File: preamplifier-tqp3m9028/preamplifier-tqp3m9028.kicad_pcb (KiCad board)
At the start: 2 copper layers, 35 x 35 mm, 19 parts, among them J101 Barrel_Jack_Switch, J102 Conn_Coaxial, J103 Conn_Coaxial, U101 AMS1117-5.0, U102 TQP3M9028

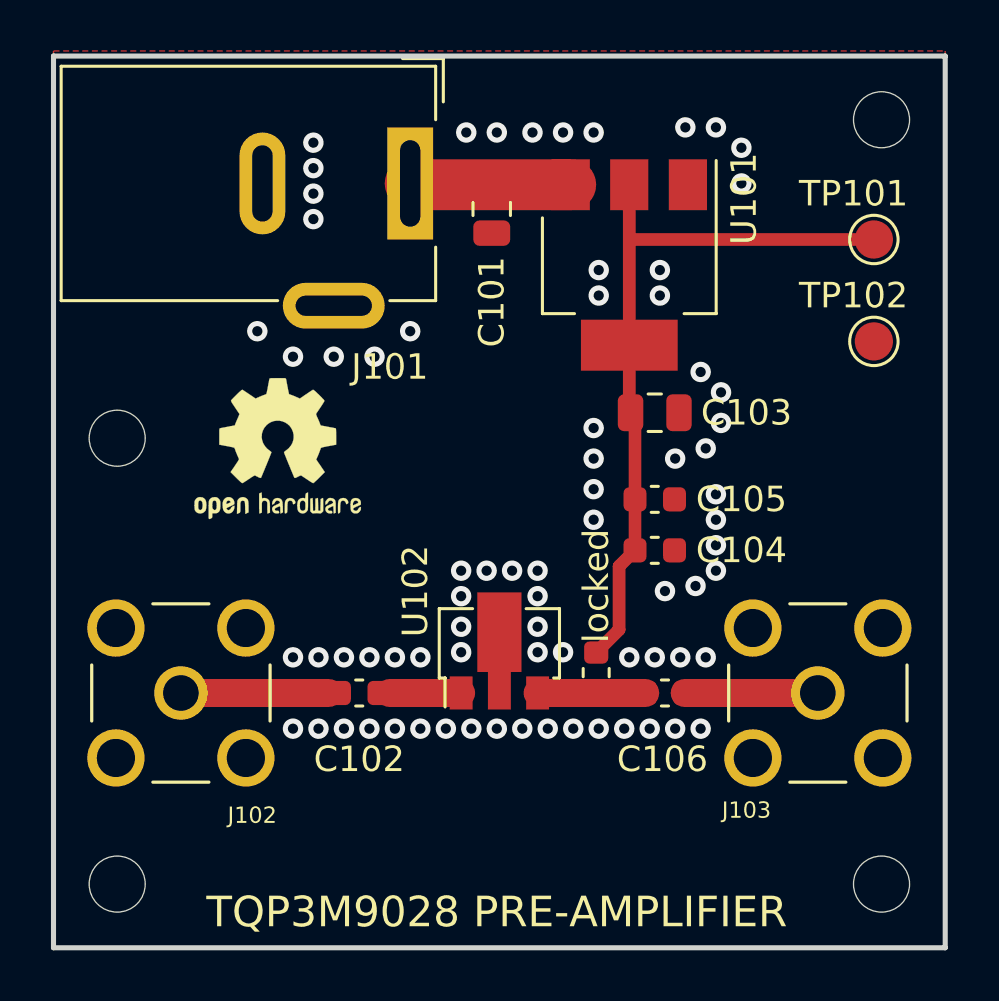
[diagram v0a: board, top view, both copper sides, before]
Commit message: Update PCB - relocate DC jack
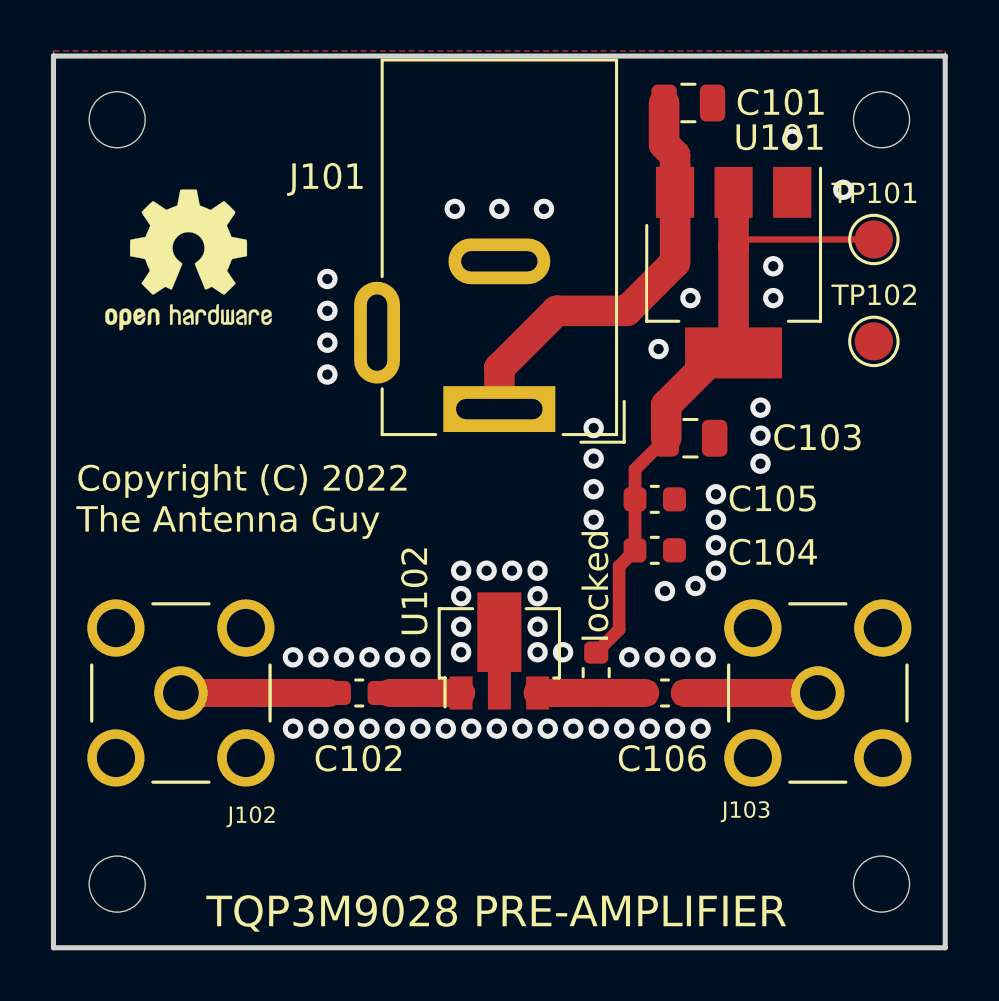
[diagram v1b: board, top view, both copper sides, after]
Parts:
- moved   12.5 mm to (102.5, 87.5)
- moved J101 9.52 mm to (117.5, 98.9), turned to 180 degrees
- moved C101 8.77 mm to (124.9, 86.8), turned to 0 degrees
- moved REF** 8.19 mm to (105.3, 93.0)
- moved U101 4.11 mm to (126.7, 93.5)
- moved C103 1.72 mm to (125.0, 100.0)
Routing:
- net Net-(C101-Pad1): track 6.39 -> 16.7 mm
- net Net-(C103-Pad1): track 28.7 -> 26.5 mm
- net GND: vias 75 -> 64
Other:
- board text added: "Copyright (C) 2022 The Antenna Guy"
- board text added: "For 500 - 4000 MHz: L101 = 68 nH C102 = C106 = 100 pF C104 = 10 nF For WLAN apps: L101 = 18 nH C102 = C106 = 22 pF C104 = 10 nF For 50 - 500 MHz: L101 = 330 nH C102 = C106 = 1000 pF C104 = 10 nF"
- board text added: "For 500 - 4000 MHz: L101 = 68 nH C102 = C106 = 100 pF For WLAN apps: L101 = 18 nH C102 = C106 = 22 pF For 50 - 500 MHz: L101 = 330 nH C102 = C106 = 1000 pF"

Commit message: Finish PCB - generate fabrication files
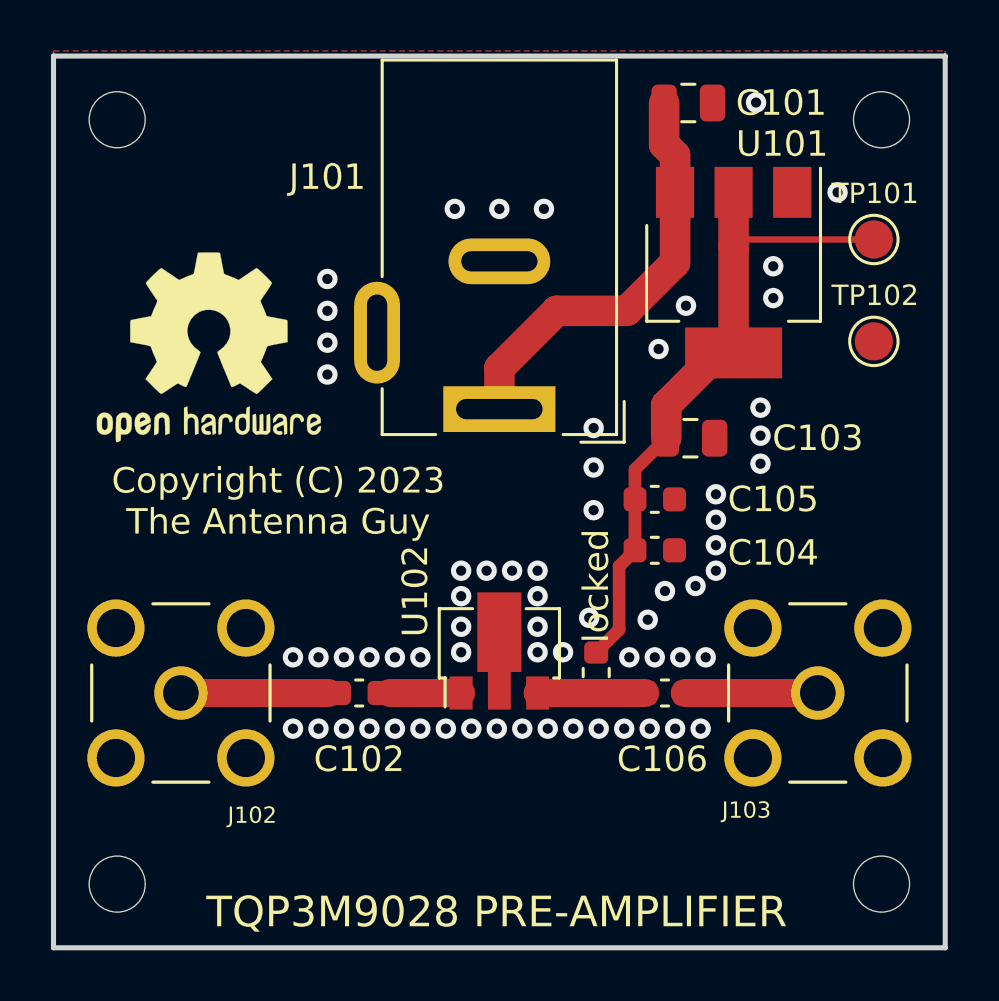
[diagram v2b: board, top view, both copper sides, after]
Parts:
- removed the REF** at (105.3, 93.0)
- added REF**: OSHW-Logo2_9.8x8mm_SilkScreen, Symbol:OSHW-Logo2_9.8x8mm_SilkScreen, F.Cu at (106.1, 96.4)
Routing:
- net GND: vias 64 -> 65
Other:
- board text added: "Copyright (C) 2023 The Antenna Guy"
- board text removed: "Copyright (C) 2022 The Antenna Guy"
